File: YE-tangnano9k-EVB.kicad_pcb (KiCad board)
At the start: 2 copper layers, 95 x 72 mm, 23 parts, among them J1 Conn_01x24_Socket, J2 Conn_01x24_Socket, Q1 2SA1015, SW1 SW_SPDT, SW2 SW_Push, SW3 SW_Push, U1 Tang Nano 9K, U2 OSL40391-IRA

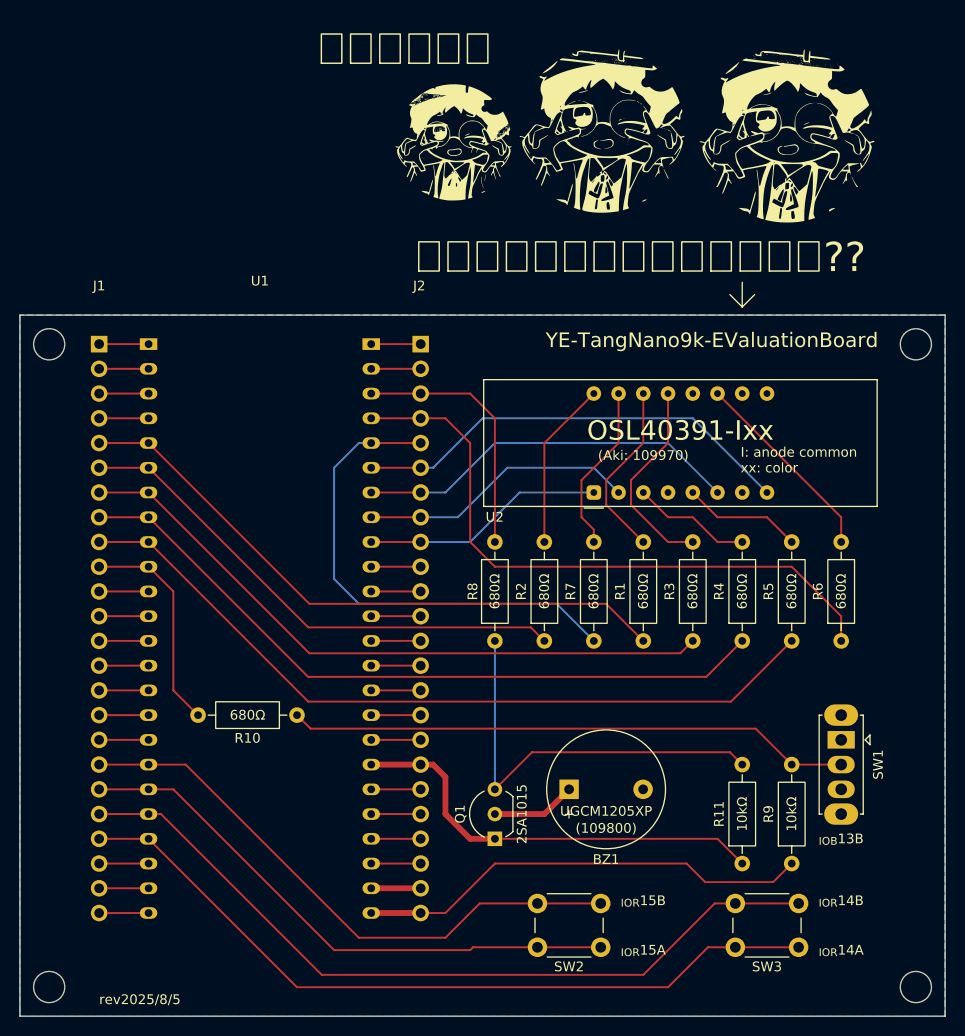
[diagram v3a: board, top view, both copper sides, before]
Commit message: change Buzzer_logic (→ActiveHIGH) fix pcb
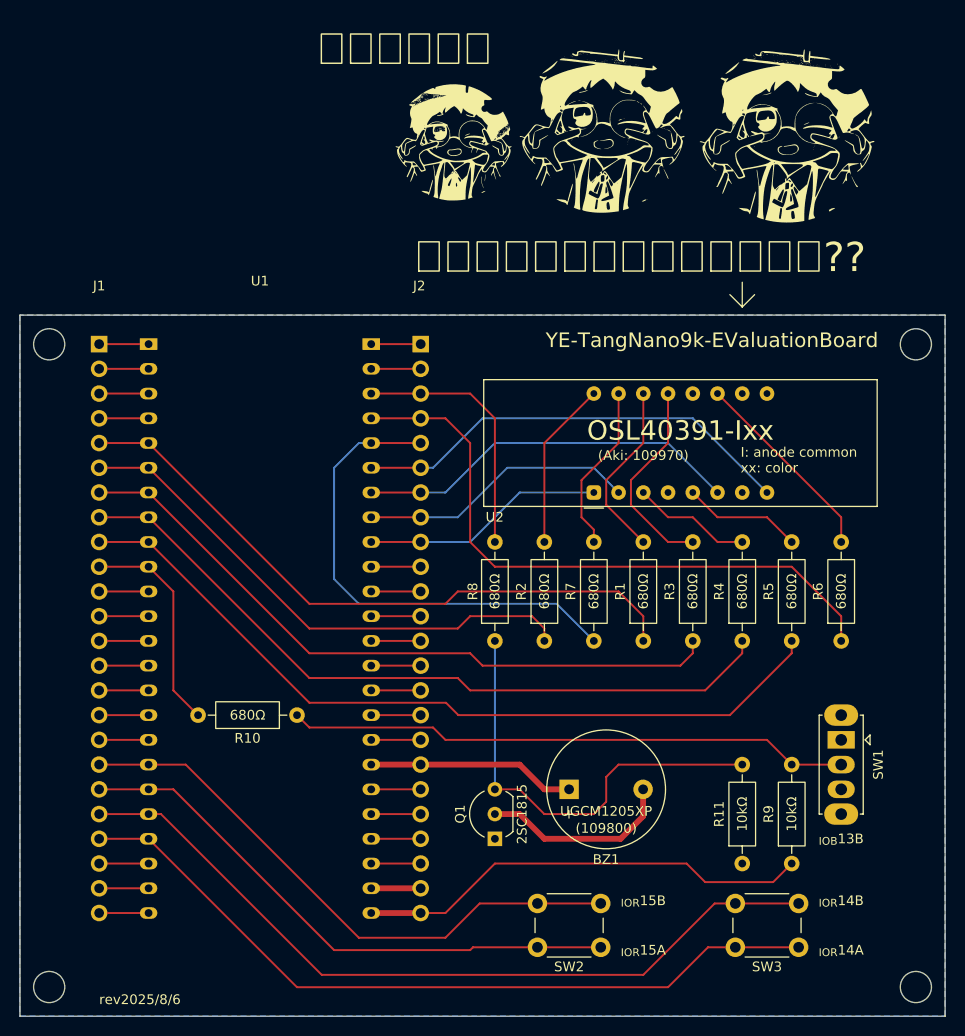
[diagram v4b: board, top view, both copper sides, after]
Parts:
- Q1: value 2SA1015 -> 2SC1815
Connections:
- BZ1 pad 1: Net-(BZ1-+) -> +5V
- BZ1 pad 2: GND -> Net-(BZ1--)
- Q1 pad 1: +5V -> GND
- Q1 pad 2: Net-(BZ1-+) -> Net-(BZ1--)
- R11 pad 1: +5V -> GND
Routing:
- net +5V: track 44.5 -> 21.4 mm
- net Net-(BZ1--): track 0.00 -> 20.0 mm
- net Net-(BZ1-+): track 8.67 -> 0.00 mm
- net Net-(Q1-B): track 42.7 -> 45.3 mm
- net /seg_a: track 64.3 -> 66.8 mm
- net /seg_d: track 74.4 -> 76.3 mm
- net /seg_e: track 80.5 -> 82.4 mm
- net /seg_b: track 53.1 -> 54.9 mm
- net /seg_c: track 68.3 -> 70.1 mm
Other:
- board text added: "rev2025/8/6"
- board text removed: "rev2025/8/5"
